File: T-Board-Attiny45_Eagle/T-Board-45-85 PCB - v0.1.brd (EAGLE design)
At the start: 41.9 x 47 mm, 18 parts, among them IC1 LD117MIRROR, IC4 NCP1117MIRROR, J1 POWER_JACKPTH, J2 AVR_SPI_PRG_6PTH, U1 TINY45-20-DIP

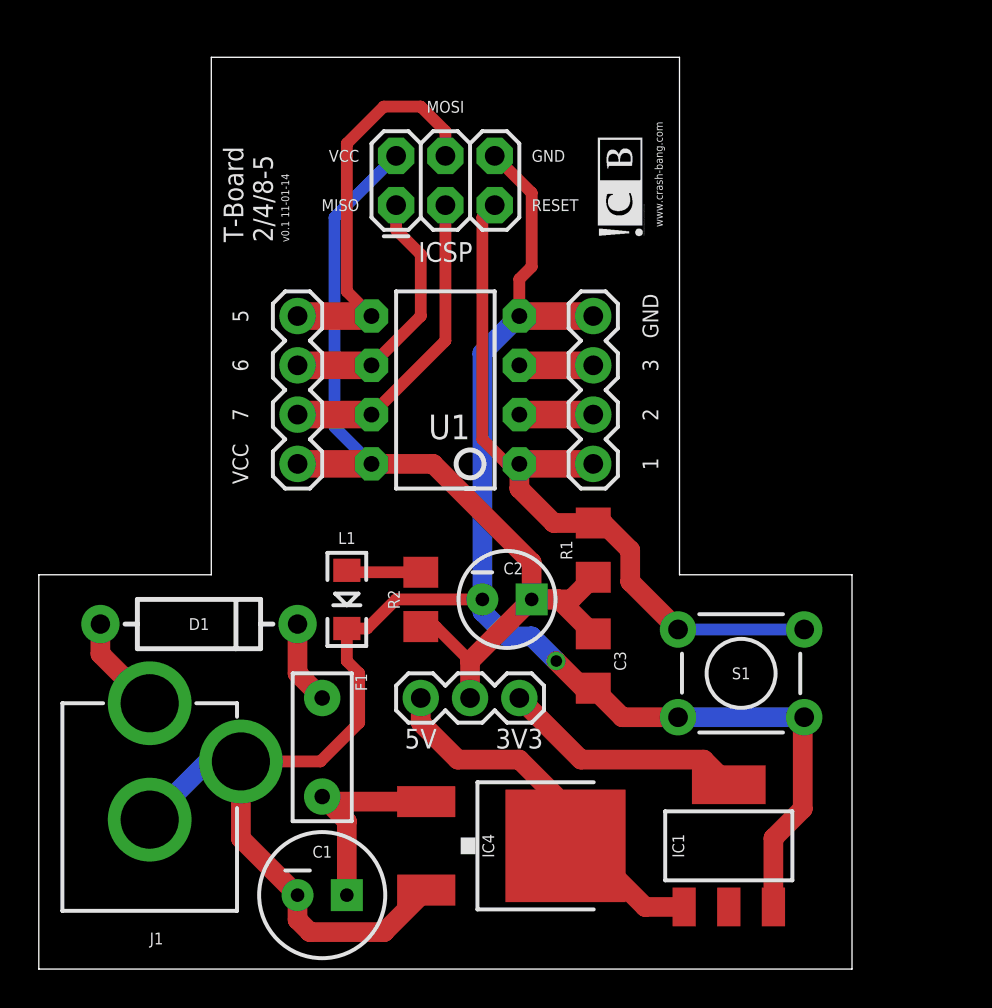
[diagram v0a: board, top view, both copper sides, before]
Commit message: v0.2 - 2-sided prototype
2-sided prototype send to OSHPark to fab.  Includes:
- ICSP header
- Consistency in trace width
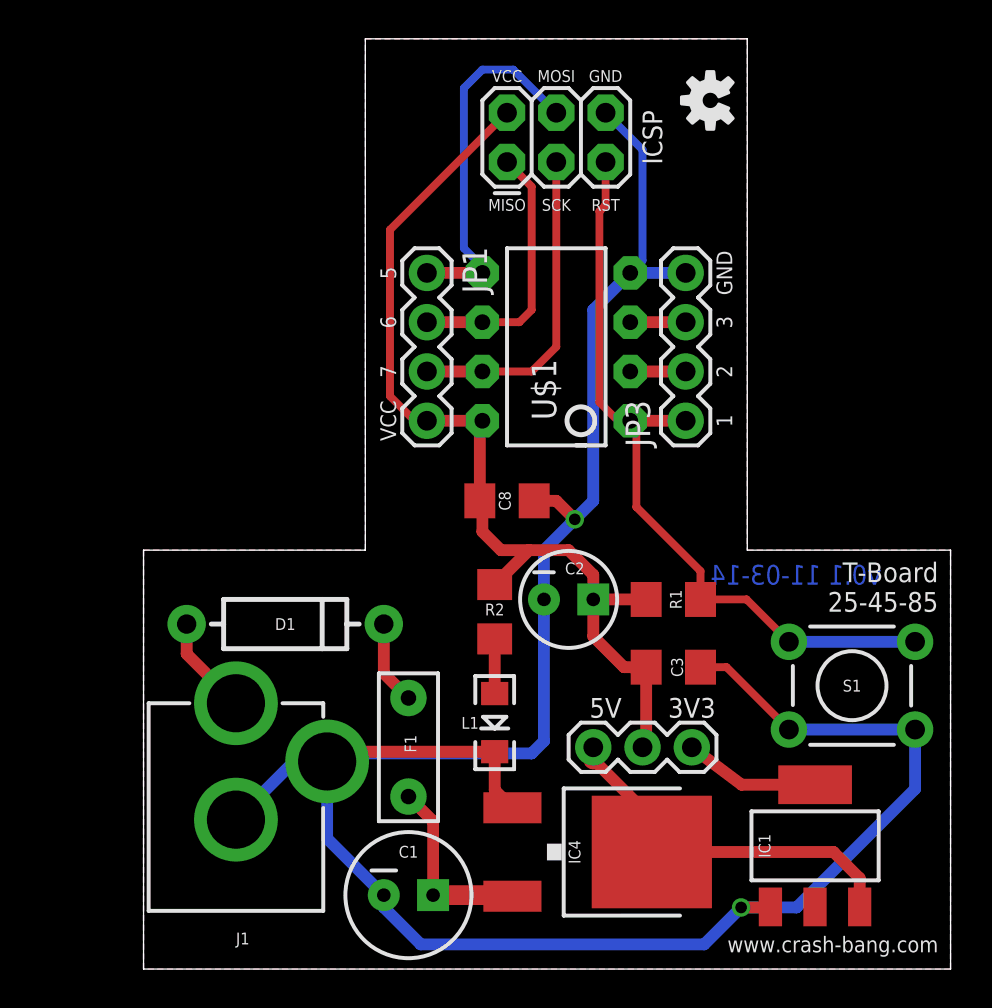
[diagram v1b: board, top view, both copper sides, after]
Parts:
- removed U1: TINY45-20-DIP, SparkFun-DigitalIC:DIP08
- added C8: 100nF, SparkFun-Passives:1206
- added LOGO1: OSHW-LOGOS, SparkFun-Aesthetics:OSHW-LOGO-S
- IC1: value LD117MIRROR -> LD11733TRS
- IC4: value NCP1117MIRROR -> NCP1117DT50GDT
- JP1: value Pin 1-4 -> Pin 5-8
- JP3: value Pin 5-8 -> Pin 1-4
- U$1: device CrashBang_Logo:CB_LOGO -> SparkFun-DigitalIC:DIP08
- moved JP3 20.7 mm to (33.3, 28.3), turned to 90 degrees
- moved JP1 13.1 mm to (20.0, 35.9), turned to 270 degrees
- moved LED1 9.92 mm to (23.5, 12.7)
- moved JP2 9.25 mm to (28.6, 11.4)
- moved U$1 7.24 mm to (26.7, 32.1)
- moved J2 6.13 mm to (24.1, 41.6)
- moved S1 5.75 mm to (41.9, 14.6)
- moved R1 4.85 mm to (32.7, 19.1), turned to 180 degrees
- moved IC4 4.46 mm to (29.2, 6.03)
- moved C1 4.45 mm to (19.1, 3.81)
- moved F1 4.45 mm to (19.1, 11.4)
- moved IC1 4.45 mm to (40.0, 6.35)
- moved J1 4.45 mm to (10.2, 0.00)
- moved D1 4.44 mm to (12.7, 17.8)
- moved C3 4.14 mm to (32.7, 15.6), turned to 0 degrees
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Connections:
- removed net X1: JP1.2, U1.2
- removed net X2: JP1.3, U1.3
- new net N$6: JP3.2, U$1.2
- new net N$7: JP3.3, U$1.3
- net 5V: now also IC1.3; no longer IC1.1
- net GND: now also C8.1, IC1.1, IC4.1, JP3.4, U$1.4; no longer IC1.3, IC4.3, JP1.4, U1.4
- net MISO: now also JP1.2, U$1.6; no longer JP3.2, U1.6
- net MOSI: now also JP1.1, U$1.5; no longer JP3.1, U1.5
- net N$4: now also IC4.3; no longer IC4.1
- net RESET: now also JP3.1, R1.1, U$1.1; no longer JP1.1, R1.2, U1.1
- net SCK: now also JP1.3, U$1.7; no longer JP3.3, U1.7
- net VCC: now also C8.2, JP1.4, R1.2, U$1.8; no longer JP3.4, R1.1, U1.8
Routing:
- net GND: track 101.2 -> 127.5 mm, vias 1 -> 2
- net N$10: track 12.6 -> 7.00 mm
- net X2: track 3.81 -> 0.00 mm
- net X1: track 3.81 -> 0.00 mm
- net N$7: track 0.00 -> 2.86 mm
- net N$6: track 0.00 -> 2.86 mm
- net MOSI: track 20.9 -> 18.9 mm
- net RESET: track 38.5 -> 40.0 mm
- net N$4: track 11.1 -> 9.75 mm
- net N$9: track 3.85 -> 2.82 mm
- net 5V: track 20.2 -> 19.4 mm
- net SCK: track 16.2 -> 16.7 mm
- added copper zone on layer 1, net GND
- added copper zone on layer 16, net GND
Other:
- board size 41.9 x 47 mm -> 41.6 x 47.9 mm
- board text added: "RST"
- board text added: "SCK"
- board text added: "T-Board 25-45-85"
- board text added: "v0.1 11-03-14"
- board text removed: "RESET"
- board text removed: "T-Board 2/4/8-5"
- board text removed: "v0.1 11-01-14"

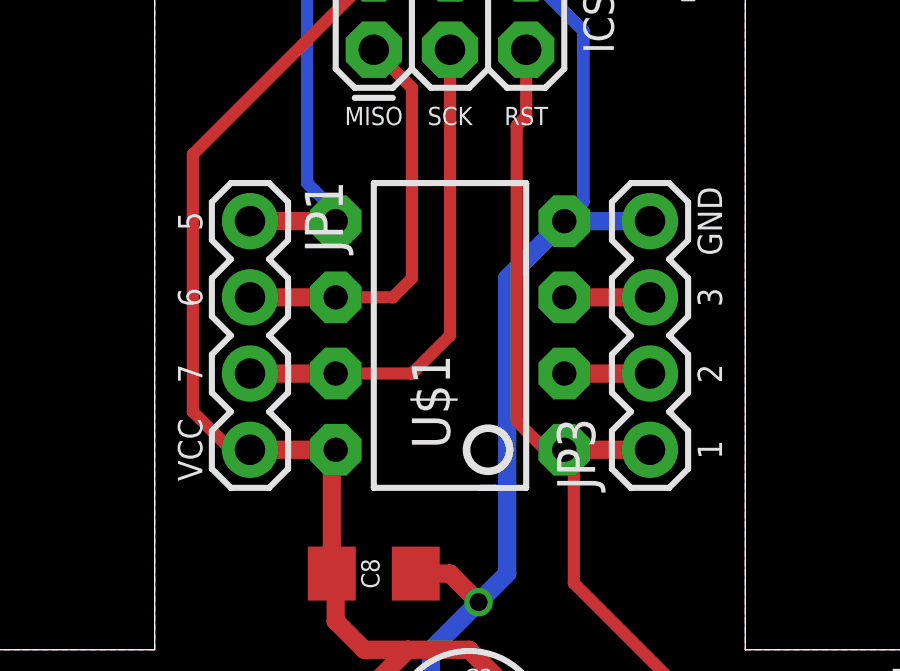
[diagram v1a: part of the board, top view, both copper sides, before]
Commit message: Adjusted header pins
Header pins spacing corrected to fit breadboard more precisely
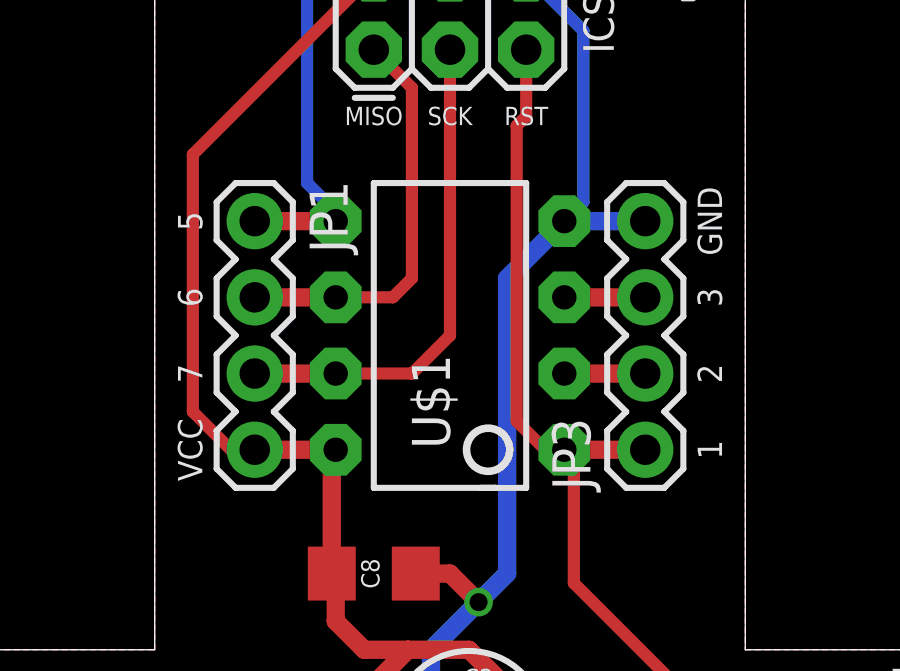
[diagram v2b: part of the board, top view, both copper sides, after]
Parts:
- moved JP1 0.16 mm to (20.2, 35.9)
- moved JP3 0.16 mm to (33.2, 28.3)
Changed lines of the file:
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@@
 <setting verticaltext="up"/>
 </settings>
-<grid distance="12.5" unitdist="mil" unit="mil" style="lines" multiple="1" display="yes" altdistance="12.5" altunitdist="mil" altunit="mil"/>
+<grid distance="0.15875" unitdist="mm" unit="mm" style="lines" multiple="1" display="yes" altdistance="0.15875" altunitdist="mm" altunit="mm"/>
 <layers>
 <layer number="1" name="Top" color="4" fill="1" visible="yes" active="yes"/>
@@
 <attribute name="NAME" x="25.4" y="31.4325" size="1.27" layer="25" ratio="10" rot="R270"/>
 </element>
-<element name="JP1" library="AndyTallack" package="1X04" value="Pin 5-8" x="20.0025" y="35.8775" rot="R270"/>
-<element name="JP3" library="AndyTallack" package="1X04" value="Pin 1-4" x="33.3375" y="28.2575" rot="R90"/>
+<element name="JP1" library="AndyTallack" package="1X04" value="Pin 5-8" x="20.16125" y="35.8775" rot="R270"/>
+<element name="JP3" library="AndyTallack" package="1X04" value="Pin 1-4" x="33.17875" y="28.2575" rot="R90"/>
 </elements>
 <signals>
@@
 <contactref element="U$1" pad="4"/>
 <contactref element="JP3" pad="4"/>
-<wire x1="33.3375" y1="35.8775" x2="30.48" y2="35.8775" width="0.6096" layer="16"/>
+<wire x1="33.17875" y1="35.8775" x2="30.48" y2="35.8775" width="0.6096" layer="16"/>
 <wire x1="26.035" y1="19.05" x2="26.035" y2="21.59" width="0.6096" layer="16"/>
 <wire x1="26.035" y1="21.59" x2="27.6225" y2="23.1775" width="0.6096" layer="16"/>
@@
 <contactref element="U$1" pad="8"/>
 <contactref element="JP1" pad="4"/>
-<wire x1="20.0025" y1="28.2575" x2="22.86" y2="28.2575" width="0.6096" layer="1"/>
+<wire x1="20.16125" y1="28.2575" x2="22.86" y2="28.2575" width="0.6096" layer="1"/>
 <wire x1="25.27" y1="21.59" x2="23.8125" y2="21.59" width="0.6096" layer="1"/>
 <wire x1="23.8125" y1="21.59" x2="22.86" y2="22.5425" width="0.6096" layer="1"/>
@@
 <wire x1="18.0975" y1="38.1" x2="18.0975" y2="29.5275" width="0.4064" layer="1"/>
 <wire x1="18.0975" y1="29.5275" x2="19.3675" y2="28.2575" width="0.4064" layer="1"/>
-<wire x1="19.3675" y1="28.2575" x2="20.0025" y2="28.2575" width="0.4064" layer="1"/>
+<wire x1="19.3675" y1="28.2575" x2="20.16125" y2="28.2575" width="0.4064" layer="1"/>
 </signal>
 <signal name="5V">
@@
 <contactref element="U$1" pad="7"/>
 <contactref element="JP1" pad="3"/>
-<wire x1="20.0025" y1="30.7975" x2="22.86" y2="30.7975" width="0.6096" layer="1"/>
+<wire x1="20.16125" y1="30.7975" x2="22.86" y2="30.7975" width="0.6096" layer="1"/>
 <wire x1="26.67" y1="32.0675" x2="25.4" y2="30.7975" width="0.4064" layer="1"/>
 <wire x1="25.4" y1="30.7975" x2="22.86" y2="30.7975" width="0.4064" layer="1"/>
@@
 <contactref element="U$1" pad="6"/>
 <contactref element="JP1" pad="2"/>
-<wire x1="20.0025" y1="33.3375" x2="22.86" y2="33.3375" width="0.6096" layer="1"/>
+<wire x1="20.16125" y1="33.3375" x2="22.86" y2="33.3375" width="0.6096" layer="1"/>
 <wire x1="25.4" y1="33.9725" x2="24.765" y2="33.3375" width="0.4064" layer="1"/>
 <wire x1="24.765" y1="33.3375" x2="22.86" y2="33.3375" width="0.4064" layer="1"/>
@@
 <contactref element="U$1" pad="5"/>
 <contactref element="JP1" pad="1"/>
-<wire x1="20.0025" y1="35.8775" x2="22.86" y2="35.8775" width="0.6096" layer="1"/>
+<wire x1="20.16125" y1="35.8775" x2="22.86" y2="35.8775" width="0.6096" layer="1"/>
 <wire x1="26.67" y1="44.1325" x2="24.4475" y2="46.355" width="0.4064" layer="16"/>
 <wire x1="24.4475" y1="46.355" x2="22.86" y2="46.355" width="0.4064" layer="16"/>
@@
 <contactref element="U$1" pad="1"/>
 <contactref element="JP3" pad="1"/>
-<wire x1="30.48" y1="28.2575" x2="33.3375" y2="28.2575" width="0.6096" layer="1"/>
+<wire x1="30.48" y1="28.2575" x2="33.17875" y2="28.2575" width="0.6096" layer="1"/>
 <wire x1="34.1025" y1="19.05" x2="34.1025" y2="20.5075" width="0.4064" layer="1"/>
 <wire x1="34.1025" y1="20.5075" x2="30.7975" y2="23.8125" width="0.4064" layer="1"/>
@@
 <contactref element="JP3" pad="2"/>
 <contactref element="U$1" pad="2"/>
-<wire x1="30.48" y1="30.7975" x2="33.3375" y2="30.7975" width="0.6096" layer="1"/>
+<wire x1="30.48" y1="30.7975" x2="33.17875" y2="30.7975" width="0.6096" layer="1"/>
 </signal>
 <signal name="N$7">
 <contactref element="JP3" pad="3"/>
 <contactref element="U$1" pad="3"/>
-<wire x1="30.48" y1="33.3375" x2="33.3375" y2="33.3375" width="0.6096" layer="1"/>
+<wire x1="30.48" y1="33.3375" x2="33.17875" y2="33.3375" width="0.6096" layer="1"/>
 </signal>
 </signals>
